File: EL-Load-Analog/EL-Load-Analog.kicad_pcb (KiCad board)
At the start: 4 copper layers, 185 x 95 mm, 299 parts, among them J1 Temp Sensor PCB, J2 SWEB8094AU-SW, J3 Conn_02x06_Odd_Even, J4 Conn_02x08_Odd_Even, J5 SWEB8094AU-RT, J7 Conn_01x02_Socket, J8 Conn_02x08_Odd_Even, J9 Temp Sensor heatsink, K2 EE2-5TNU, Q1 2N7002, Q101 TIP42C, Q2 2N7002, Q201 2N7002, Q202 2N7002, Q203 IRFP250M, Q204 IRFP250M, Q205 2N7002, Q206 2N7002, Q207 IRFP250M, Q208 IRFP250M, Q3 MMBT5551, Q301 2N7002, Q4 MMBT3904, Q5 MMBT5401, Q6 MMBT5551, U1 SN74LVC1G3157DBV, U10 TL072/OPA2376, U11 DAC8555, U12 DAC8555, U15 TPS7A2030, U17 TPS72325, U18 MCP6V51, U19 MCP6V51, U20 ADS131M02, U201 LM318D, U202 LM318D, U203 MCP6V51/LTC2050HV, U204 MCP6V51/LTC2050HV, U205 LM318D, U206 LM318D, U207 MCP6V51/LTC2050HV, U208 MCP6V51/LTC2050HV, U21 LT1964-5, U22 AMS1117, U23 TLV1117-50, U301 LM833, U302 LM833, U303 OPA189/MCP6V51/LTC2050HV, U304 OPA189/MCP6V51/LTC2050HV, U305 74HCT02, U306 LM393, U4 REF5025AD, U401 AD8038, U402 LM393, U403 74HCT02, U5 24LC32, U8 VO1400AEFTR, U9 VO1400AEFTR, X3 DIB Pheriperal connector

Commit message: Added heatsink moutingholes, reverse polarity, moved snubbers.
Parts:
- added Q7: AOSP66923, Package_SO:SO-8_3.9x4.9mm_P1.27mm, B.Cu at (43.3, 96.9)
- added R25: 0, Resistor_SMD:R_0805_2012Metric, F.Cu at (57.9, 99.6)
- added R39: 10k, Resistor_SMD:R_0805_2012Metric, F.Cu at (51.8, 87.4)
- added R46: 20k, Resistor_SMD:R_0805_2012Metric, F.Cu at (93.9, 88.9)
- added R47: 20k, Resistor_SMD:R_0805_2012Metric, F.Cu at (94.2, 73.6)
- added R48: 20k, Resistor_SMD:R_0805_2012Metric, F.Cu at (101.5, 73.6)
- added TP1: -5V, TestPoint:TestPoint_Loop_D1.80mm_Drill1.0mm_Beaded, F.Cu at (207.8, 98.8)
- added TP10: 3V, TestPoint:TestPoint_Pad_1.0x1.0mm, F.Cu at (148.9, 88.9)
- added TP11: -1V, TestPoint:TestPoint_Pad_1.0x1.0mm, F.Cu at (112.6, 98.8)
- added TP12: 2V5, TestPoint:TestPoint_Pad_1.0x1.0mm, F.Cu at (137.6, 99.5)
- added TP13: Umon, TestPoint:TestPoint_Pad_1.0x1.0mm, F.Cu at (88.6, 85.0)
- added TP14: loopSet, TestPoint:TestPoint_Pad_1.0x1.0mm, F.Cu at (169.6, 71.2)
- added TP2: +5V, TestPoint:TestPoint_Loop_D1.80mm_Drill1.0mm_Beaded, F.Cu at (207.8, 102.5)
- added TP3: GND, TestPoint:TestPoint_Loop_D2.50mm_Drill1.0mm, F.Cu at (207.8, 112.9)
- added TP4: Imon3, TestPoint:TestPoint_Pad_1.0x1.0mm, F.Cu at (69.7, 69.8)
- added TP5: Imon1, TestPoint:TestPoint_Pad_1.0x1.0mm, F.Cu at (206.4, 71.9)
- added TP6: Imon4, TestPoint:TestPoint_Pad_1.0x1.0mm, F.Cu at (120.8, 68.3)
- added TP7: Imon2, TestPoint:TestPoint_Pad_1.0x1.0mm, F.Cu at (207.7, 74.0)
- added TP8: Imon, TestPoint:TestPoint_Pad_1.0x1.0mm, F.Cu at (175.2, 93.2)
- added TP9: -2V5, TestPoint:TestPoint_Pad_1.0x1.0mm, F.Cu at (156.3, 90.8)
- D203: value 1.5KE100A smd variant -> 1.5KE100A (smd)
- moved R2 81.3 mm to (77.9, 23.0), turned to 180 degrees
- moved C3 64.2 mm to (54.3, 23.2), turned to 0 degrees
- moved R22 5.80 mm to (32.9, 52.8), turned to -90 degrees
- moved R42 5.07 mm to (37.0, 52.0), turned to 0 degrees
- moved Q5 4.04 mm to (40.5, 51.7)
- moved Q6 4.00 mm to (37.0, 55.1)
- moved C5 3.90 mm to (40.5, 55.0)
- moved R8 3.66 mm to (40.5, 57.1)
- moved R43 3.04 mm to (35.3, 58.1), turned to 0 degrees
- moved R9 2.84 mm to (40.5, 59.3), turned to 180 degrees
- moved D203 2.52 mm to (47.2, 23.6)
- moved R23 2.01 mm to (57.9, 97.6)
- moved Q3 1.74 mm to (30.1, 49.4)
- moved C6 1.61 mm to (30.1, 52.5)
- moved J9 1.55 mm to (84.0, 24.9)
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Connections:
- net Net-(J5-Pin_1) renamed LoadPlusUnfused
- C310 pad 2: Net-(U306A-+) -> /Monitoring, Crossover, Von/scaledUmon
- J2 pad 1: LoadMin -> Net-(J2-Pin_1)
- J4 pad 8: +15V -> ReversePolarity
- NT202 pad 2: LoadMin -> Net-(J2-Pin_1)
- R1 pad 2: Net-(U306A-+) -> /Monitoring, Crossover, Von/scaledUmon
- R23 pad 1: LoadMin -> Net-(J2-Pin_1)
- R321 pad 2: Net-(U306A-+) -> /Monitoring, Crossover, Von/scaledUmon
- U306 pad 3: Net-(U306A-+) -> /Monitoring, Crossover, Von/scaledUmon
- U306 pad 5: GND -> /Monitoring, Crossover, Von/scaledUmon
- U306 pad 6: GND -> GCOM
- U306 pad 7: unconnected-(U306-Pad7) -> /MOSFET Loops/ReverseProt
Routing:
- net /MOSFET Loops/ReverseProt: track 0.00 -> 72.9 mm, vias 0 -> 3
- net LoadMin: track 422.1 -> 458.3 mm, vias 5 -> 8
- net Net-(J2-Pin_1): track 0.00 -> 35.4 mm
- net ReversePolarity: track 0.00 -> 32.9 mm
- net Net-(D206-K): track 198.1 -> 227.5 mm
- net LoadPlus: track 574.4 -> 602.0 mm
- net GCOM: track 230.1 -> 256.9 mm, vias 8 -> 10
- net +12V: track 339.7 -> 364.6 mm, vias 6 -> 9
- net /Monitoring, Crossover, Von/scaledUmon: track 0.00 -> 16.6 mm
- net Net-(U306A-+): track 11.1 -> 0.00 mm
- net Umon: track 128.5 -> 135.8 mm, vias 3 -> 4
- net Net-(Q5-B): track 15.0 -> 21.5 mm
- net -2V5: track 34.8 -> 40.5 mm
- net GND: track 360.2 -> 354.8 mm, vias 236 -> 225
- net Net-(R225-Pad2): track 124.5 -> 129.6 mm
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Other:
- board text added: "+12V"

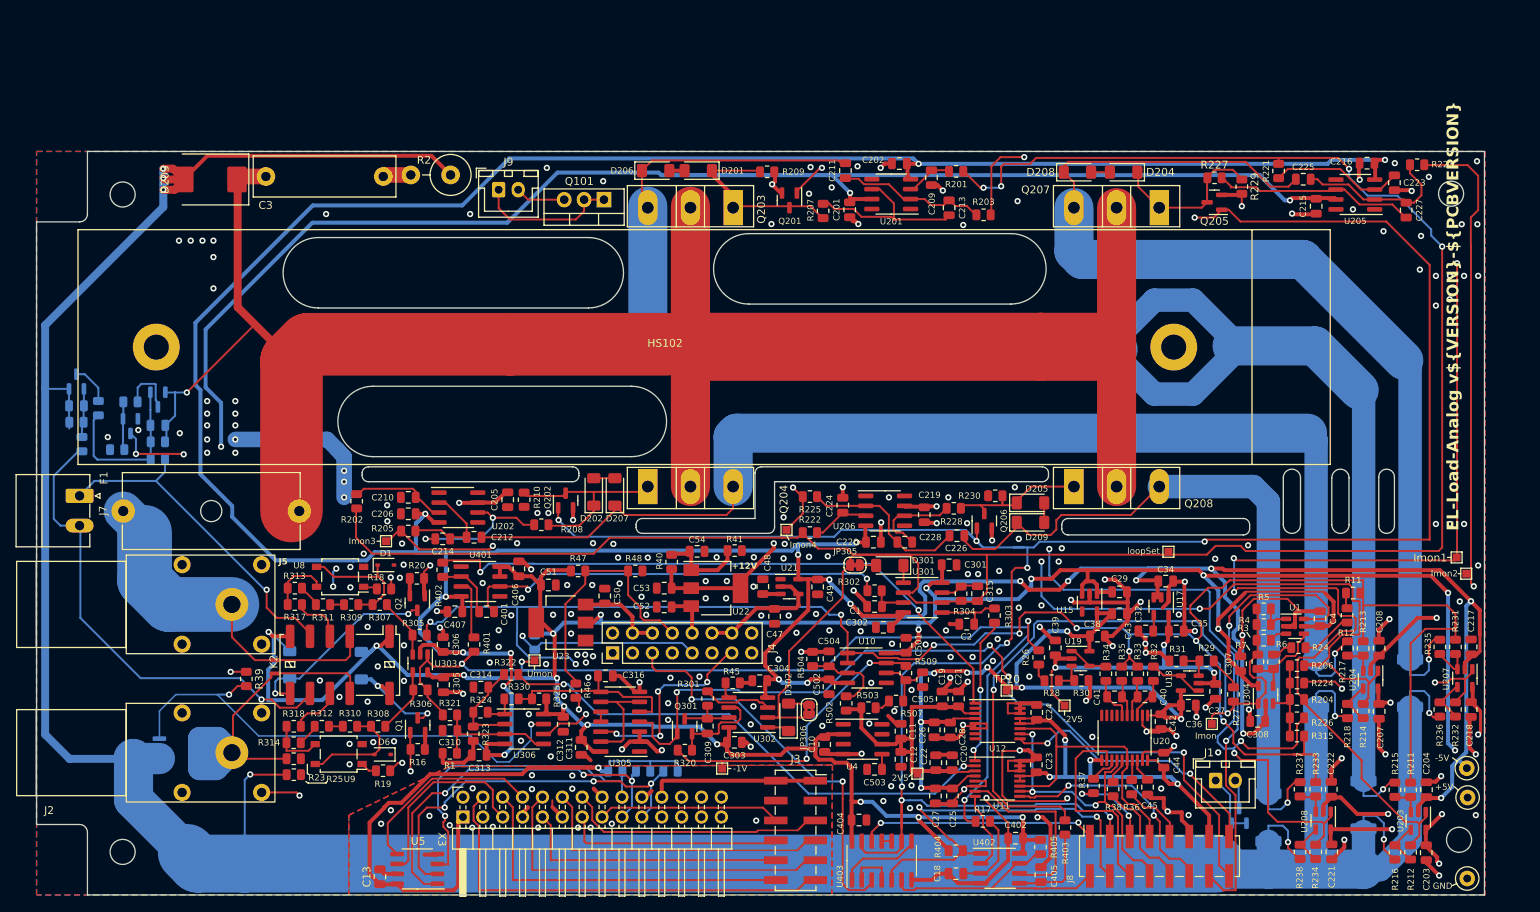
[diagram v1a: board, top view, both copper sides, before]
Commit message: v4 Analog board design. Features reverse polarity, remote sense error and new clamping circuitry.
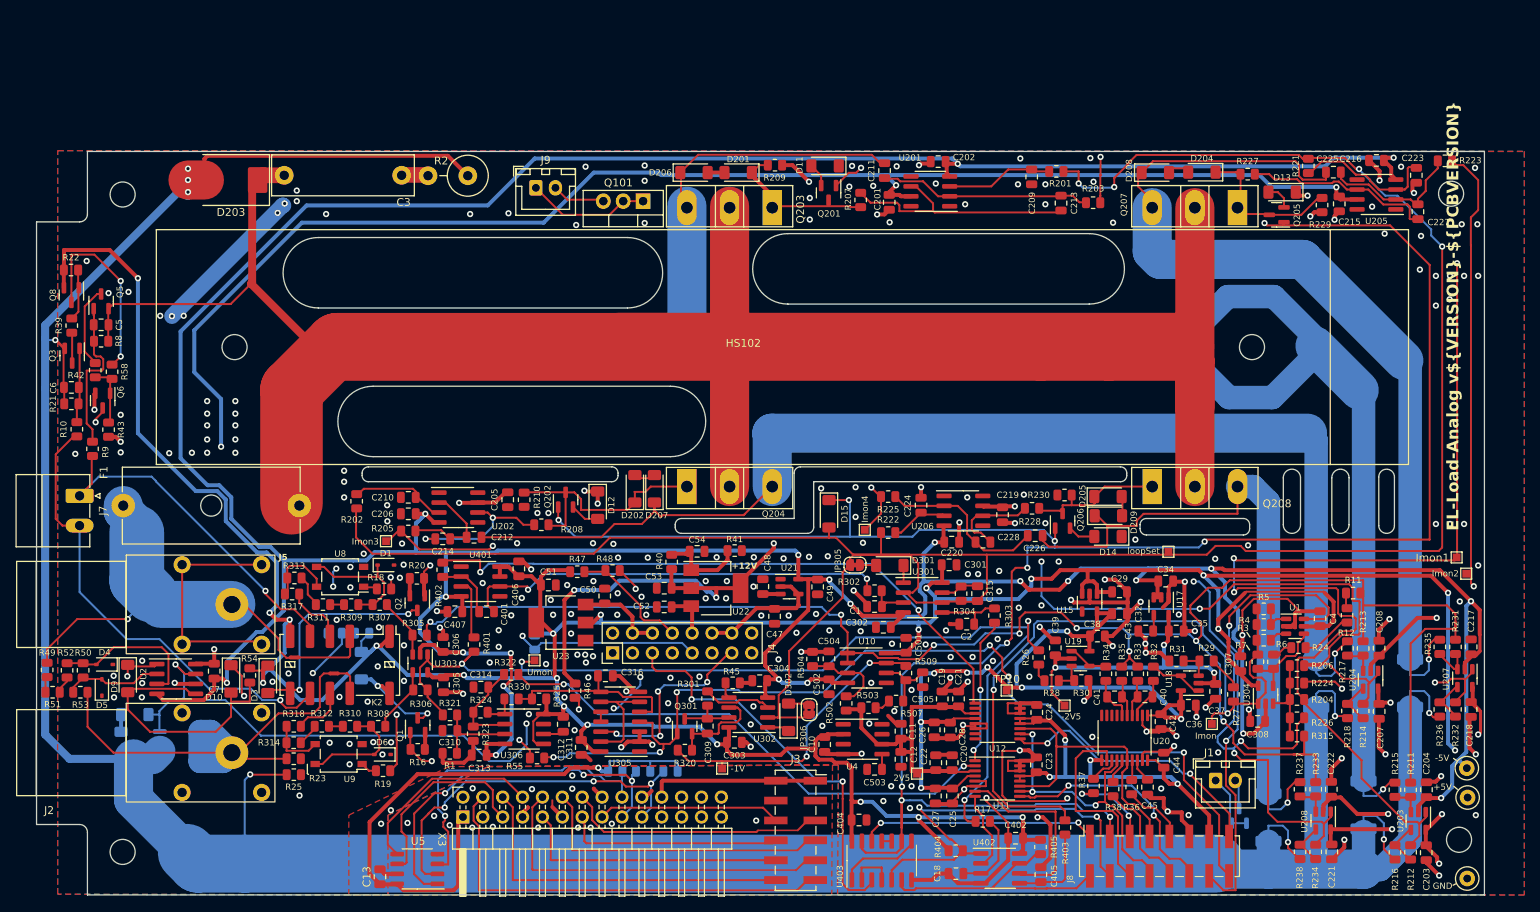
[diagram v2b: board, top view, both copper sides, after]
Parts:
- added C7: 100n, Capacitor_SMD:C_0805_2012Metric, F.Cu at (47.7, 86.4)
- added D10: 1N4148, Diode_SMD:D_MiniMELF, F.Cu at (49.9, 87.4)
- added D11: 1N4148, Diode_SMD:D_MiniMELF, F.Cu at (125.8, 21.9)
- added D12: 1N4148, Diode_SMD:D_MiniMELF, F.Cu at (96.7, 65.2)
- added D13: 1N4148, Diode_SMD:D_MiniMELF, F.Cu at (184.2, 25.2)
- added D14: 1N4148, Diode_SMD:D_MiniMELF, F.Cu at (161.9, 69.2)
- added D15: 1N4148, Diode_SMD:D_MiniMELF, F.Cu at (126.2, 66.3)
- added D4: PESD3V3L1BAF, Diode_SMD:D_SOD-323, F.Cu at (33.7, 85.5)
- added D5: PESD3V3L1BAF, Diode_SMD:D_SOD-323, F.Cu at (33.4, 88.5)
- added D7: TZMB16-GS08, Diode_SMD:D_MiniMELF, B.Cu at (37.5, 92.0)
- added D8: TZMB16-GS08, Diode_SMD:D_MiniMELF, B.Cu at (35.8, 95.9)
- added D9: 1N4148, Diode_SMD:D_MiniMELF, F.Cu at (36.6, 87.3)
- added OSHWLogo1: CERN-OHL-W-2.0, Symbol:OSHW-Logo_5.7x6mm_SilkScreen, B.Cu at (195.2, 35.1)
- added Q8: MMBT5401, Package_TO_SOT_SMD:SOT-23, F.Cu at (29.4, 38.4)
- added R49: 1M, Resistor_SMD:R_0805_2012Metric, F.Cu at (26.4, 86.2)
- added R50: 100k, Resistor_SMD:R_0805_2012Metric, F.Cu at (30.9, 86.3)
- added R51: 1M, Resistor_SMD:R_0805_2012Metric, F.Cu at (27.1, 89.1)
- added R52: 1M, Resistor_SMD:R_0805_2012Metric, F.Cu at (28.9, 86.3)
- added R53: 100k, Resistor_SMD:R_0805_2012Metric, F.Cu at (30.6, 89.1)
- added R54: 100k, Resistor_SMD:R_0805_2012Metric, F.Cu at (52.2, 87.0)
- added R55: 10k, Resistor_SMD:R_0805_2012Metric, F.Cu at (89.0, 97.5)
- added R56: 10k, Resistor_SMD:R_0805_2012Metric, B.Cu at (66.6, 81.5)
- added R57: 10k, Resistor_SMD:R_0805_2012Metric, B.Cu at (63.1, 81.5)
- added R58: 22k, Resistor_SMD:R_0805_2012Metric, F.Cu at (34.6, 48.1)
- added U2: LM393, Package_SO:SOIC-8_3.9x4.9mm_P1.27mm, F.Cu at (42.9, 87.4)
- C5, C6, D3, Q3, Q5, Q6, R43: moved to F.Cu
- R10, R9: value 22k -> 750; moved to F.Cu
- R21, R8: value 10k -> 330; moved to F.Cu
- R22: value 22k -> 47k; moved to F.Cu
- R39: value 10k -> 22k
- R42: value 10k -> 22k; moved to F.Cu
- R46: value 20k -> 10k
- R47, R48: value 20k -> 4k7
- moved R39 50.4 mm to (29.5, 42.2), turned to 90 degrees
- moved R22 18.0 mm to (29.4, 35.1), turned to 180 degrees
- moved C5 14.8 mm to (33.2, 42.1)
- moved R8 14.8 mm to (33.2, 44.2)
- moved Q5 14.5 mm to (33.2, 39.1), turned to 90 degrees
- moved C213 14.3 mm to (155.9, 26.6)
- moved R203 14.1 mm to (160.0, 26.6)
- moved C209 12.8 mm to (152.2, 23.2)
- moved R201 12.8 mm to (155.3, 22.6)
- moved R229 10.5 mm to (189.2, 26.9)
- moved C219 10.0 mm to (148.4, 66.4)
- moved C220 10.0 mm to (141.9, 69.9)
- moved C224 10.0 mm to (138.0, 65.2)
- moved C226 10.0 mm to (152.6, 69.1)
- moved C228 10.0 mm to (145.9, 69.9)
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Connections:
- net Net-(J2-Pin_1) renamed LoadMinDirect
- net Net-(R324-Pad1) renamed VonComp
- Q201 pad 2: GND -> Net-(D11-A)
- Q202 pad 2: GND -> Net-(D12-A)
- Q205 pad 2: GND -> Net-(D13-A)
- Q206 pad 2: GND -> Net-(D14-A)
- Q7 pad 4: /MOSFET Loops/ReverseProt -> /CV, OVP & OCP/ReverseProt
- R22 pad 1: Net-(Q3-C) -> Net-(Q8-B)
- R22 pad 2: Net-(Q5-B) -> +5V
- R39 pad 1: +12V -> Net-(Q3-C)
- R39 pad 2: /MOSFET Loops/ReverseProt -> Net-(Q8-B)
- R46 pad 1: /MOSFET Loops/ReverseProt -> /CV, OVP & OCP/ReverseProt
- R46 pad 2: ReversePolarity -> +12V
- R48 pad 1: GND -> Net-(D9-K)
- U306 pad 5: /Monitoring, Crossover, Von/scaledUmon -> +5V
- U306 pad 6: GCOM -> GND
- U306 pad 7: /MOSFET Loops/ReverseProt -> unconnected-(U306-Pad7)
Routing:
- net Net-(D9-K): track 0.00 -> 93.8 mm, vias 0 -> 4
- net LoadPlus: track 602.0 -> 695.0 mm, vias 1 -> 0
- net +5V: track 474.7 -> 556.7 mm, vias 24 -> 27
- net /CV, OVP & OCP/ReverseProt: track 0.00 -> 75.8 mm, vias 0 -> 3
- net /MOSFET Loops/ReverseProt: track 72.9 -> 0.00 mm, vias 3 -> 0
- net GND: track 354.8 -> 425.4 mm, vias 225 -> 254
- net Net-(D10-K): track 0.00 -> 47.6 mm, vias 0 -> 2
- net LoadPlusUnfused: track 32.8 -> 75.1 mm, vias 0 -> 1
- net Net-(D10-A): track 0.00 -> 34.2 mm
- net -5V: track 612.7 -> 644.5 mm, vias 23 -> 24
- net LoadMinDirect: track 35.4 -> 67.0 mm
- net +12V: track 364.6 -> 394.9 mm, vias 9 -> 11
- net Net-(U2B--): track 0.00 -> 29.8 mm, vias 0 -> 2
- net GCOM: track 256.9 -> 230.1 mm, vias 10 -> 8
- net Net-(Q8-C): track 0.00 -> 25.0 mm, vias 0 -> 2
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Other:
- outline, holes or cut-outs redrawn
- board text added: "https://github.com/fietser28/EL-Load"

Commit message: Schema changed to 4.1, PCB version E. Modified R44, Remote sense error circtuit had wrong min input.
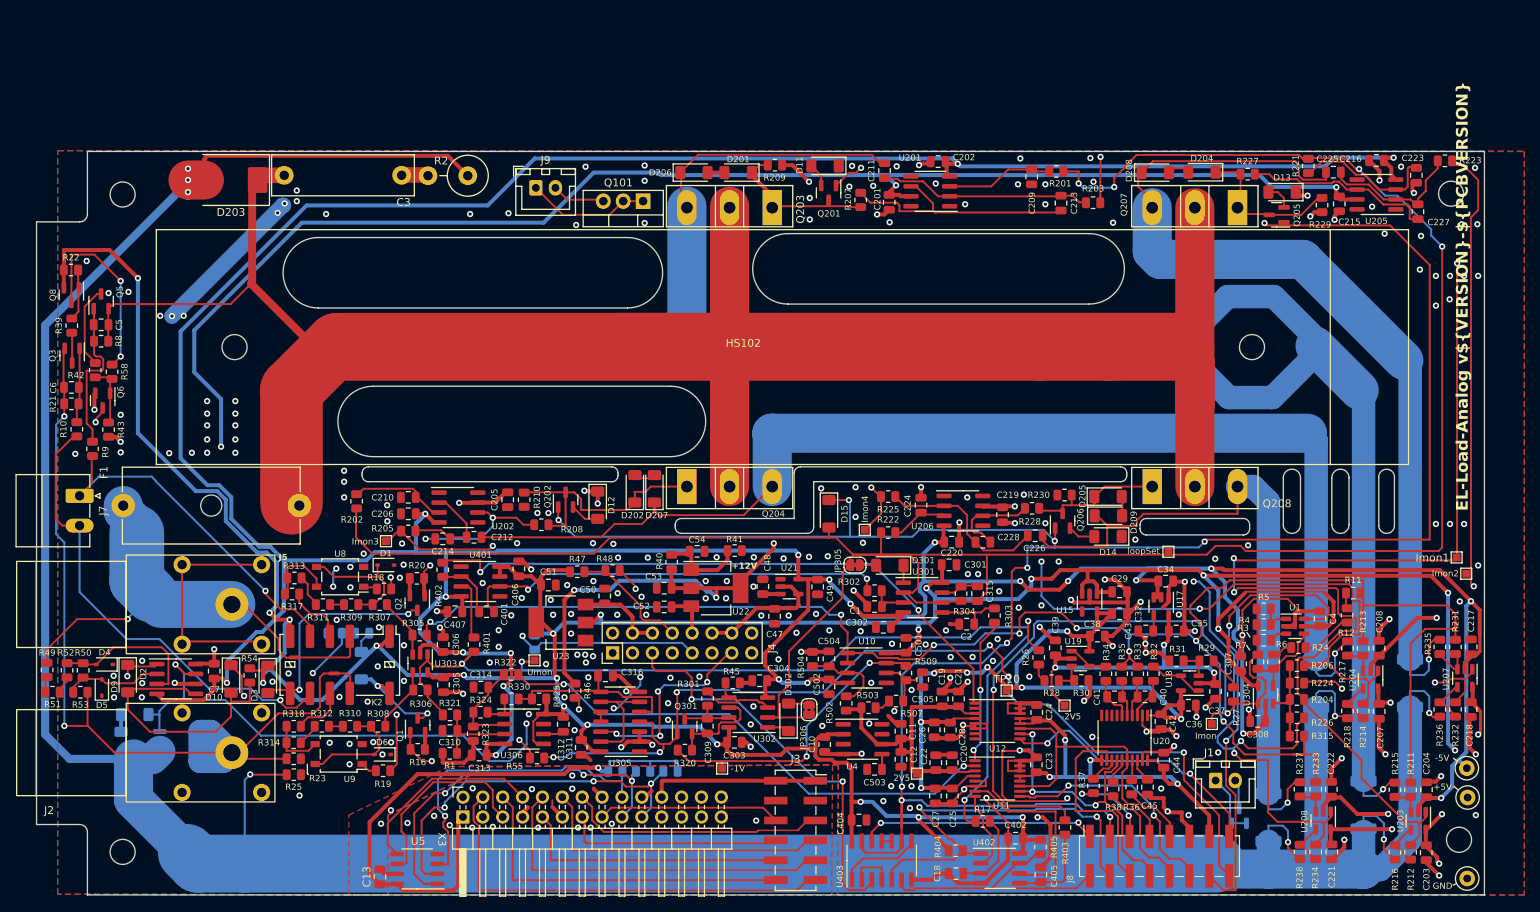
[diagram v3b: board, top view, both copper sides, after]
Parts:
- OSHWLogo1: footprint Symbol:OSHW-Logo_5.7x6mm_SilkScreen -> Symbol:OSHW-Logo_7.5x8mm_SilkScreen
- R44: value 10k -> 4k7
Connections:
- C6 pad 1: LoadMin -> LoadMinDirect
- Q3 pad 2: LoadMin -> LoadMinDirect
- R21 pad 1: LoadMin -> LoadMinDirect
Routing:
- net LoadMinDirect: track 67.0 -> 119.0 mm, vias 0 -> 2
- net LoadMin: track 456.5 -> 444.8 mm, vias 9 -> 8
